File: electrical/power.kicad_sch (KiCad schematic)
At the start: 44 parts

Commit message: Interim check-in
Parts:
- removed 12V_CB, FLAP_CB, FUEL_PUMP_CB, LAND_TAXI_CB, SMOKE_CB: 10A, symbol flyerx:Circuit_Breaker
- removed ALT_CB: 60A, symbol flyerx:Circuit_Breaker
- removed AVIONICS_CB, BAK_CB, MAIN_CB: 20A, symbol flyerx:Circuit_Breaker
- removed BAK_BAT, MAIN_BAT: Battery, symbol Device:Battery
- removed BAK_BAT_VOLTS_FS, FUEL_LT_FS: 1, symbol Device:Fuse
- removed BAK_SW, MAIN_SW: ~, symbol Switch:SW_SPST
- removed G5_CB, GDU4XX_CB, GPS175_CB, GSA28_PWR: 5A, symbol flyerx:Circuit_Breaker
- removed GAD27_CB, GEA24_CB, GMU11_CB, GSU25_CB: 2A, symbol flyerx:Circuit_Breaker
- removed GDL52_PWR, GTX320_CB, POSITION_CB, STROBE_CB: 3A, symbol flyerx:Circuit_Breaker
- removed GTR20_CB: 7.5A, symbol flyerx:Circuit_Breaker
- removed MISC_CB, TAILBCN_CB: 1A, symbol flyerx:Circuit_Breaker
- added 12V_CB, FLAP_CB, FUEL_PUMP_CB, IGN_CB, LAND_TAXI_CB, SMOKE_CB: 10A, symbol Device:CircuitBreaker_1P_US
- added AVIONICS_CB: 20A, symbol Device:CircuitBreaker_1P_US
- added FPP: DT2P, symbol Connector:Conn_01x02_Socket
- added FPR: DT2R, symbol Connector:Conn_01x02_Pin
- added FUEL_PUMP_ON_R: 1K 1W, symbol Device:R_US
- added G5_CB, GDU4XX_CB, GPS175_CB, GSA28_PWR, IGN_BAK_CB: 5A, symbol Device:CircuitBreaker_1P_US
- added GAD27_CB, GEA24_CB, GMU11_CB, GSU25_CB: 2A, symbol Device:CircuitBreaker_1P_US
- added GDL52_PWR, GTX320_CB, POSITION_CB, STROBE_CB: 3A, symbol Device:CircuitBreaker_1P_US
- added GMC507_FS1: 1, symbol Device:Fuse
- added GTR20_CB: 7.5A, symbol Device:CircuitBreaker_1P_US
- added IGN_BAK: ~, symbol flyerx:TCW_IBBS-12V-3AH
- added IGN_BAK_SW: ~, symbol Switch:SW_SPST
- added MISC_CB, TAILBCN_CB: 1A, symbol Device:CircuitBreaker_1P_US
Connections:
- net 12V_PWR: now also 12V_CB.2
- net ELT_PWR: now also MISC_CB.2
- net ENCODER_PWR: now also GTX320_CB.2
- net FLAP_PWR: now also FLAP_CB.2
- net FUEL_PUMP_PWR: now also FUEL_PUMP_CB.2
- net G5_PWR: now also G5_CB.2
- net GAD27_PWR: now also GAD27_CB.2
- net GAD29_PWR: now also GPS175_CB.2
- net GDL52_PWR: now also GDL52_PWR.2
- net GDU4XX_PWR: now also GDU4XX_CB.2
- net GEA24_PWR: now also GEA24_CB.2
- net GMU11_PWR: now also GMU11_CB.2
- net GND: now also FPR.2 (Pin_2), IGN_BAK.10 (GROUND), IGN_BAK.11 (GROUND), IGN_BAK.9 (GROUND), IGN_BAK_SW.1 (A); no longer FUEL_PUMP.2 (-)
- net GSA28_PWR: now also GMC507_FS1.1, GSA28_PWR.2
- net GSU25_PWR: now also GSU25_CB.2
- net GTR20_PWR: now also GTR20_CB.2
- net LAND_TAXI_PWR: now also LAND_TAXI_CB.2
- net POSITION_PWR: now also POSITION_CB.2
- net SMOKE_PWR: now also SMOKE_CB.2
- net STROBE_PWR: now also STROBE_CB.2
- net TAILBCN_PWR: now also TAILBCN_CB.2
- net at FUEL_PUMP.1 (+): now also FPP.1 (Pin_1); no longer FUEL_PUMP_SW.2 (B)
- net at AVIONICS_SW.2 (B): now also AVIONICS_CB.2
- new net: FPP.2 (Pin_2), FUEL_PUMP.2 (-)
- new net: IGN_BAK.1 (ENABLE_BACKUP_SWITCH), IGN_BAK_SW.2 (B)
- new net: FPR.1 (Pin_1), FUEL_PUMP_ON_R.1, FUEL_PUMP_SW.2 (B)
- new net FUEL_PUMP_ON: FUEL_PUMP_ON_R.2
- new net IGN_BAK_LOW: IGN_BAK.3 (LOW_VOLT_WARNING)
- new net IGN_BAK_PWR: IGN_BAK.5 (POWER_IN), IGN_BAK_CB.2
- new net IGN_BAK_VOLTS: IGN_BAK.2 (BATTERY_INFO)
- new net IGN_PWR: IGN_BAK.12 (POWER_OUT), IGN_BAK.13 (POWER_OUT), IGN_BAK.14 (POWER_OUT), IGN_BAK.15 (POWER_OUT), IGN_BAK.6 (PASSTHROUGH_POWER_IN), IGN_BAK.7 (PASSTHROUGH_POWER_IN), IGN_BAK.8 (PASSTHROUGH_POWER_IN), IGN_CB.2
- new net TRIM_PWR: GMC507_FS1.2
- no-connect marks 0 -> 2
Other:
- note removed: "Backup Battery Volts is to measure health of backup battery and if it needs to be charged up in-flight"
- note removed: "From existing alternator power source with contactor"
- moved on the sheet: 12V, 12V_SW, FUEL_PUMP, FUEL_PUMP_SW, POSITION_LT1, POSITION_LT2, POSITION_SW, STROBE_LT1, STROBE_LT2, STROBE_SW, USB

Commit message: Updated from learnings from N78HR
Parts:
- removed FUEL_PUMP_ON_R: 1K 1W, symbol Device:R_US
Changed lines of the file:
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@@
 	(title_block
 		(title "Power Distribution")
-		(date "2025-11-02")
+		(date "2025-11-19")
 		(rev "1.1")
 		(company "N877RV")
@@
 	)
 	(junction
-		(at 156.21 189.23)
-		(diameter 0)
-		(color 0 0 0 0)
-	)
-	(junction
 		(at 153.67 135.89)
 		(diameter 0)
@@
 	(wire
 		(pts
-			(xy 156.21 189.23) (xy 161.29 189.23)
+			(xy 147.32 189.23) (xy 161.29 189.23)
 		)
 		(stroke
@@
 	(wire
 		(pts
-			(xy 171.45 173.99) (xy 177.8 173.99)
-		)
-		(stroke
-			(width 0)
-			(type default)
-		)
-	)
-	(wire
-		(pts
 			(xy 165.1 231.14) (xy 170.18 231.14)
 		)
@@
 	(wire
 		(pts
-			(xy 163.83 173.99) (xy 156.21 173.99)
-		)
-		(stroke
-			(width 0)
-			(type default)
-		)
-	)
-	(wire
-		(pts
 			(xy 173.99 57.15) (xy 168.91 57.15)
 		)
@@
 		)
 	)
-	(wire
-		(pts
-			(xy 147.32 189.23) (xy 156.21 189.23)
-		)
-		(stroke
-			(width 0)
-			(type default)
-		)
-	)
 	(bus
 		(pts
@@
 	(wire
 		(pts
-			(xy 156.21 173.99) (xy 156.21 189.23)
-		)
-		(stroke
-			(width 0)
-			(type default)
-		)
-	)
-	(wire
-		(pts
 			(xy 77.47 85.09) (xy 80.01 85.09)
 		)
@@
 		)
 	)
-	(hierarchical_label "FUEL_PUMP_ON"
-		(shape output)
-		(at 177.8 173.99 0)
-		(effects
-			(font
-				(size 1.27 1.27)
-			)
-			(justify left)
-		)
-	)
 	(hierarchical_label "G5_PWR"
 		(shape output)
@@
 					(unit 1)
 				)
-			)
-		)
-	)
-	(symbol
-		(lib_id "Device:R_US")
-		(at 167.64 173.99 90)
-		(unit 1)
-		(exclude_from_sim no)
-		(in_bom yes)
-		(on_board yes)
-		(dnp no)
-		(fields_autoplaced yes)
-		(property "Reference" "FUEL_PUMP_ON_R"
-			(at 167.64 167.64 90)
-			(effects
-				(font
-					(size 1.27 1.27)
-				)
-			)
-		)
-		(property "Value" "1K 1W"
-			(at 167.64 170.18 90)
-			(effects
-				(font
-					(size 1.27 1.27)
-				)
-			)
-		)
-		(property "Footprint" ""
-			(at 167.894 172.974 90)
-			(effects
-				(font
-					(size 1.27 1.27)
-				)
-				(hide yes)
-			)
-		)
-		(property "Datasheet" "~"
-			(at 167.64 173.99 0)
-			(effects
-				(font
-					(size 1.27 1.27)
-				)
-				(hide yes)
-			)
-		)
-		(property "Description" "Resistor, US symbol"
-			(at 167.64 173.99 0)
-			(effects
-				(font
-					(size 1.27 1.27)
-				)
-				(hide yes)
-			)
-		)
-		(pin "2"
-		)
-		(pin "1"
-		)
-		(instances
-			(project "electrical"
-				(path "/e8ec215a-dbe2-4eba-a577-e50a0a128049/2852c073-fbc9-4469-a6bf-ba3e911c7f5a"
-					(reference "FUEL_PUMP_ON_R")
-					(unit 1)
-				)

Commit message: Interim check-in
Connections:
- net White: now reaches FPR.1 (Pin_1), FUEL_PUMP_SW.2 (B)
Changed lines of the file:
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@@
 	(wire
 		(pts
-			(xy 151.13 191.77) (xy 161.29 191.77)
+			(xy 149.86 191.77) (xy 161.29 191.77)
 		)
 		(stroke
@@
 			(width 0)
 			(type default)
+		)
+	)
+	(label "White{slash}Blue"
+		(at 161.29 191.77 180)
+		(effects
+			(font
+				(size 1.27 1.27)
+			)
+			(justify right bottom)
+		)
+	)
+	(label "White"
+		(at 161.29 189.23 180)
+		(effects
+			(font
+				(size 1.27 1.27)
+			)
+			(justify right bottom)
 		)
 	)
@@
 	(global_label "GND"
 		(shape passive)
-		(at 151.13 191.77 180)
+		(at 149.86 191.77 180)
 		(fields_autoplaced yes)
 		(effects
@@
 		)
 		(property "Intersheetrefs" "${INTERSHEET_REFS}"
-			(at 145.3856 191.77 0)
-			(effects
-				(font
+			(at 144.1156 191.77 0)
+			(effects
+				(font

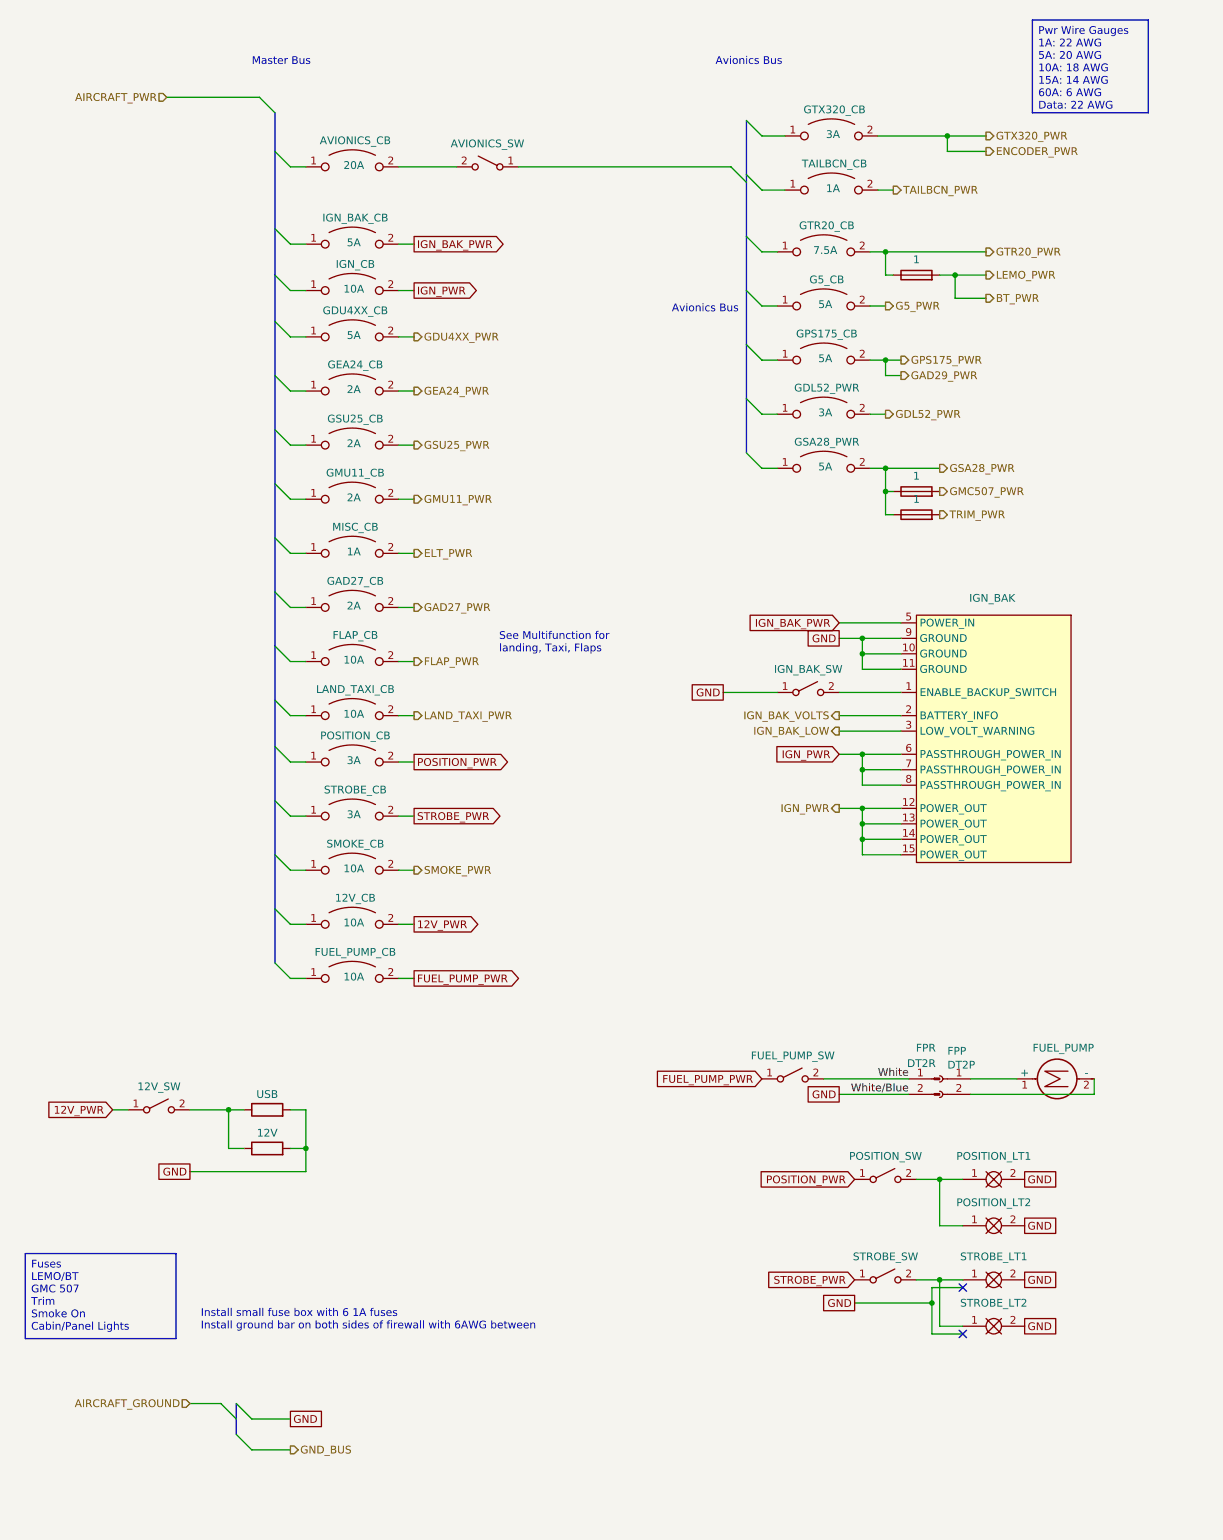
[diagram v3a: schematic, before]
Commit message: Went through and changed a lot from discussions and tradeoffs. Added GTX 330, rmemoved Connext from GDU and added to GPS 175 from GDL 52. Added relay for smoke and to not use GAD 27. Added Tach sensor for SureFly. Added carb heat. Added connectors to run panel disconnected.
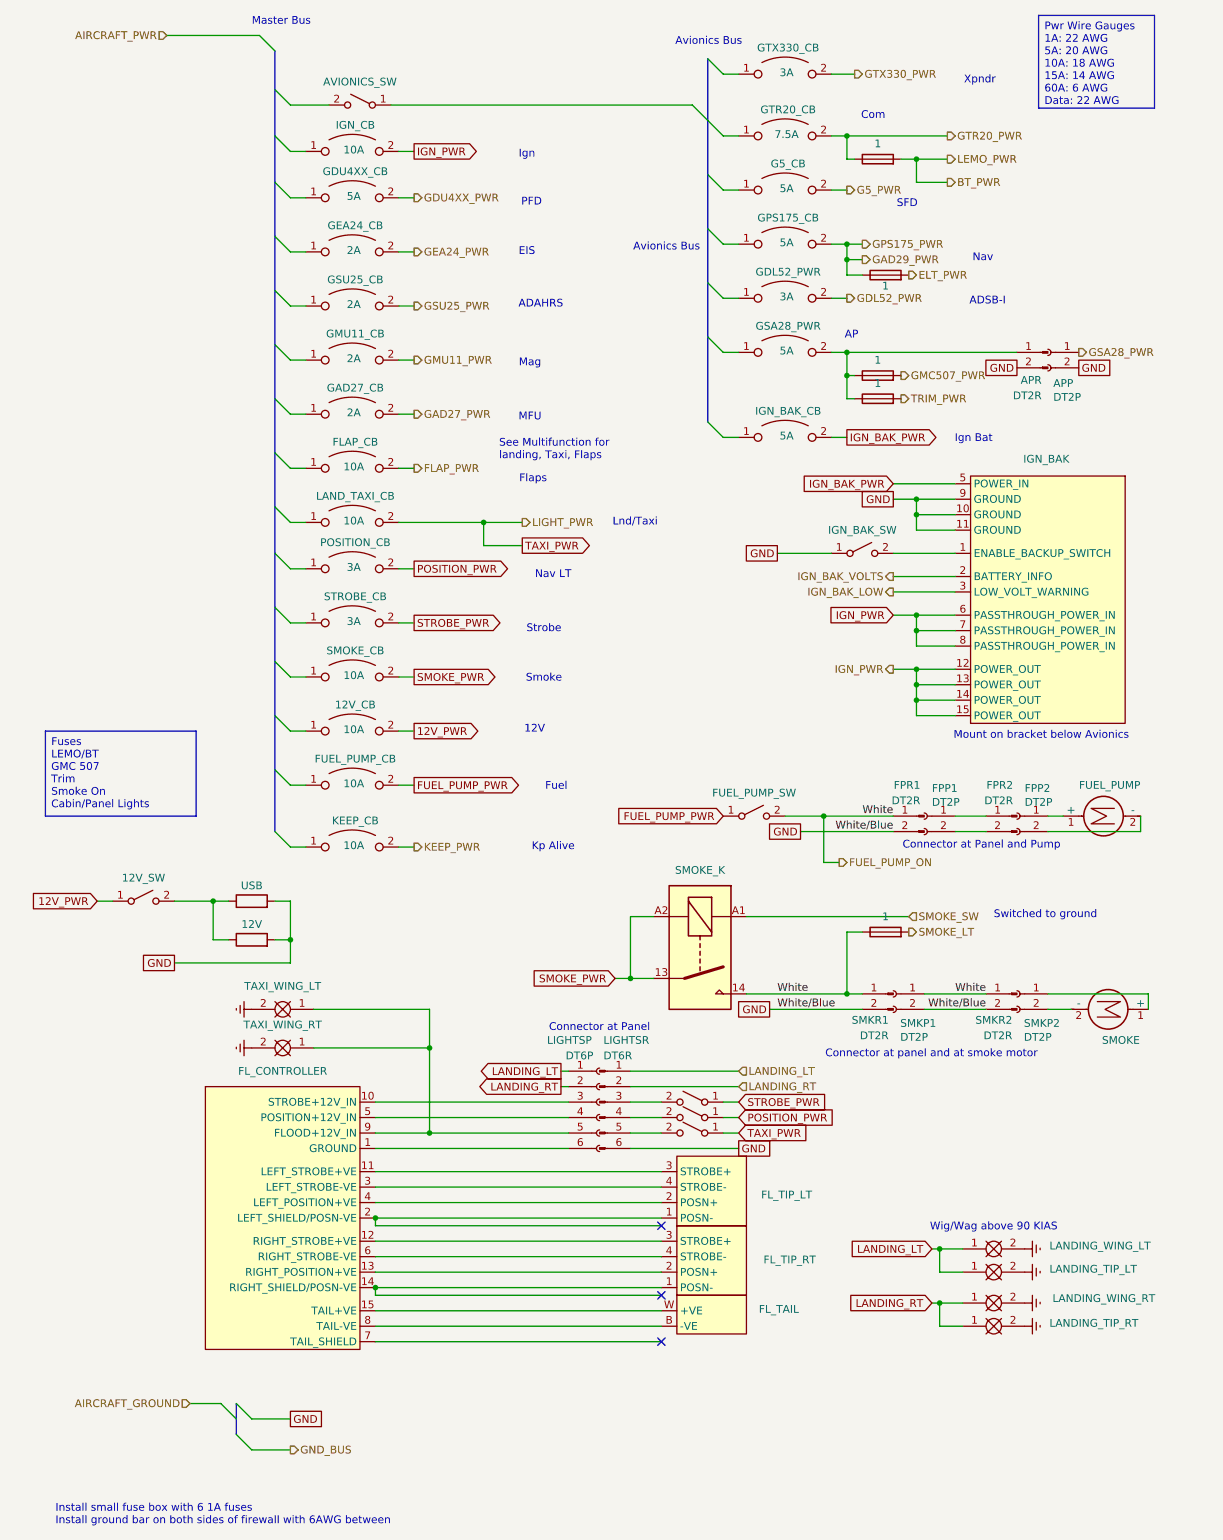
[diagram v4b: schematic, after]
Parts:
- removed AVIONICS_CB: 20A, symbol Device:CircuitBreaker_1P_US
- removed MISC_CB, TAILBCN_CB: 1A, symbol Device:CircuitBreaker_1P_US
- removed POSITION_LT1, POSITION_LT2, STROBE_LT1, STROBE_LT2: Clear, symbol FlyerX:Bulb
- added APP, FPP2, SMKP1, SMKP2: DT2P, symbol Connector:Conn_01x02_Socket
- added APR, FPR2, SMKR1, SMKR2: DT2R, symbol Connector:Conn_01x02_Pin
- added FL_CONTROLLER: ~, symbol flyerx:Flyleds_Strobe_Controller
- added FL_TAIL: ~, symbol flyerx:Flyleds_Tail_Module
- added FL_TIP_LT, FL_TIP_RT: ~, symbol flyerx:Flyleds_Wing_Module
- added KEEP_CB: 10A, symbol Device:CircuitBreaker_1P_US
- added LANDING_TIP_LT, LANDING_TIP_RT, LANDING_WING_LT, LANDING_WING_RT: ~, symbol flyerx:Bulb
- added LEMO_FS1, SMOKE_LT_FS: 1, symbol Device:Fuse
- added LIGHTSP: DT6P, symbol Connector:Conn_01x06_Socket
- added LIGHTSR: DT6R, symbol Connector:Conn_01x06_Pin
- added SMOKE: Motor_DC, symbol Motor:Motor_DC
- added SMOKE_K: Relay_SPST-NO, symbol Relay:Relay_SPST-NO
- added TAXI_SW: ~, symbol Switch:SW_SPST
- added TAXI_WING_LT, TAXI_WING_RT: Clear, symbol FlyerX:Bulb
- renumbered FPP to FPP1, FPR to FPR1, GTX320_CB to GTX330_CB
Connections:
- net ELT_PWR: now also LEMO_FS1.2
- net GAD29_PWR: now also LEMO_FS1.1
- net GND: now also APP.2 (Pin_2), APR.2 (Pin_2), LIGHTSR.6 (Pin_6), SMKP1.2 (Pin_2), SMKR1.2 (Pin_2), SMKR2.2 (Pin_2)
- net GSA28_PWR: now also APP.1 (Pin_1); no longer GMC507_FS.1, GMC507_FS1.1, GSA28_PWR.2
- net SMOKE_PWR: now also SMOKE_K.13, SMOKE_K.A2
- net at FUEL_PUMP.1 (+): now also FPP2.1 (Pin_1); no longer FPP1.1 (Pin_1)
- net at FUEL_PUMP.2 (-): now also FPP2.2 (Pin_2); no longer FPP1.2 (Pin_2)
- net at STROBE_SW.2 (B): now also LIGHTSR.3 (Pin_3)
- net at POSITION_SW.2 (B): now also LIGHTSR.4 (Pin_4)
- net ENCODER_PWR renamed GTX330_PWR
- net LAND_TAXI_PWR renamed TAXI_PWR
- net TAXI_PWR: now also TAXI_SW.1 (A)
- net White renamed FUEL_PUMP_ON
- net FUEL_PUMP_ON: now also SMKP1.1 (Pin_1), SMKR1.1 (Pin_1), SMKR2.1 (Pin_1), SMOKE_K.14, SMOKE_LT_FS.1
- new net: FPP1.1 (Pin_1), FPR2.1 (Pin_1)
- new net: FPP1.2 (Pin_2), FPR2.2 (Pin_2)
- new net: APR.1 (Pin_1), GMC507_FS.1, GMC507_FS1.1, GSA28_PWR.2
- new net: SMKP2.1 (Pin_1), SMOKE.1 (+)
- new net: SMKP2.2 (Pin_2), SMOKE.2 (-)
- new net: FL_CONTROLLER.9 (FLOOD+12V_IN), LIGHTSP.5 (Pin_5), TAXI_WING_LT.1, TAXI_WING_RT.1
- new net: FL_CONTROLLER.10 (STROBE+12V_IN), LIGHTSP.3 (Pin_3)
- new net: FL_CONTROLLER.5 (POSITION+12V_IN), LIGHTSP.4 (Pin_4)
- new net: FL_CONTROLLER.1 (GROUND), LIGHTSP.6 (Pin_6)
- new net: FL_CONTROLLER.8 (TAIL-VE), FL_TAIL.B (-VE)
- new net: FL_CONTROLLER.15 (TAIL+VE), FL_TAIL.W (+VE)
- new net: LIGHTSR.5 (Pin_5), TAXI_SW.2 (B)
- new net: FL_CONTROLLER.2 (LEFT_SHIELD/POSN-VE), FL_TIP_LT.1 (POSN-)
- new net: FL_CONTROLLER.4 (LEFT_POSITION+VE), FL_TIP_LT.2 (POSN+)
- new net: FL_CONTROLLER.11 (LEFT_STROBE+VE), FL_TIP_LT.3 (STROBE+)
- new net: FL_CONTROLLER.3 (LEFT_STROBE-VE), FL_TIP_LT.4 (STROBE-)
- new net: FL_CONTROLLER.12 (RIGHT_STROBE+VE), FL_TIP_RT.3 (STROBE+)
- new net: FL_CONTROLLER.13 (RIGHT_POSITION+VE), FL_TIP_RT.2 (POSN+)
- new net: FL_CONTROLLER.14 (RIGHT_SHIELD/POSN-VE), FL_TIP_RT.1 (POSN-)
- new net: FL_CONTROLLER.6 (RIGHT_STROBE-VE), FL_TIP_RT.4 (STROBE-)
- new net Earth: LANDING_TIP_LT.2, LANDING_TIP_RT.2, LANDING_WING_LT.2, LANDING_WING_RT.2, TAXI_WING_LT.2, TAXI_WING_RT.2
- new net KEEP_PWR: KEEP_CB.2
- new net LANDING_LT: LANDING_TIP_LT.1, LANDING_WING_LT.1, LIGHTSP.1 (Pin_1), LIGHTSR.1 (Pin_1)
- new net LANDING_RT: LANDING_TIP_RT.1, LANDING_WING_RT.1, LIGHTSP.2 (Pin_2), LIGHTSR.2 (Pin_2)
- new net SMOKE_LT: SMOKE_LT_FS.2
- new net SMOKE_SW: SMOKE_K.A1
- no-connect marks 2 -> 3
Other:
- note added: "12V"
- note added: "ADAHRS"
- note added: "ADSB-I"
- note added: "AP"
- note added: "Com"
- note added: "Connector at Panel"
- note added: "Connector at Panel and Pump"
- note added: "Connector at panel and at smoke motor"
- note added: "EIS"
- note added: "Flaps"
- note added: "Fuel"
- note added: "Ign"
- note added: "Ign Bat"
- note added: "Kp Alive"
- note added: "Lnd/Taxi"
- note added: "MFU"
- note added: "Mag"
- note added: "Mount on bracket below Avionics"
- note added: "Nav"
- note added: "Nav LT"
- note added: "PFD"
- note added: "SFD"
- note added: "Smoke"
- note added: "Strobe"
- note added: "Switched to ground"
- note added: "Wig/Wag above 90 KIAS"
- note added: "Xpndr"
- moved on the sheet: 12V, 12V_CB, 12V_SW, AVIONICS_SW, FLAP_CB, FPP1, FPR1, FUEL_PUMP, FUEL_PUMP_CB, FUEL_PUMP_SW, G5_CB, GAD27_CB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
